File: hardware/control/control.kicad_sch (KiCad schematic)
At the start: 46 parts, among them IC1 TMUX4053DYYR, J0 43045-0412, J1 Conn_01x02_Pin, J11 Conn_01x04_Pin, J12 Camera Isolated triggers (ope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, J2 Conn_01x02_Pin, J3 Conn_01x02_Pin, J4 Conn_01x02_Pin, J5 Conn_01x05_Pin, J6 Conn_01x04_Pin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

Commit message: removing old thermocouple ic
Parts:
- removed C3: 0.1uF, Capacitor_THT:C_Disc_D5.0mm_W2.5mm_P2.50mm, symbol Device:C
- removed J7: Screw_Terminal_01x02, TerminalBlock_Phoenix:TerminalBlock_Phoenix_MKDS-1,5-2_1x02_P5.00mm_Horizontal, symbol Connector:Screw_Terminal_01x02
- removed U3: MAX6675ISA_, MAX6675ISA_:SOIC127P600X175-8N, symbol MAX6675ISA_:MAX6675ISA_
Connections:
- no-connect marks 18 -> 17
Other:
- note removed: "K-Thermocouple- to-Digital Converter"
- moved on the sheet: TP5

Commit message: external spi temp chip
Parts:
- added J7: Conn_01x08_Pin, Connector_Molex:Molex_PicoBlade_53047-0810_1x08_P1.25mm_Vertical, symbol Connector:Conn_01x08_Pin
- added R11: 10k, Resistor_THT:R_Axial_DIN0207_L6.3mm_D2.5mm_P10.16mm_Horizontal, symbol Device:R
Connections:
- net +5V: now also J7.4 (Pin_4)
- net GND: now also J7.2 (Pin_2), J7.5 (Pin_5), J7.7 (Pin_7)
- net at A1.13 (D10): now also J7.6 (Pin_6)
- net at A1.14 (MOSI): now also J7.8 (Pin_8), R11.2
- net at A1.15 (MISO): now also R11.1
- net at A1.16 (SCK): now also J7.1 (Pin_1)
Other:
- moved on the sheet: J6, TP6

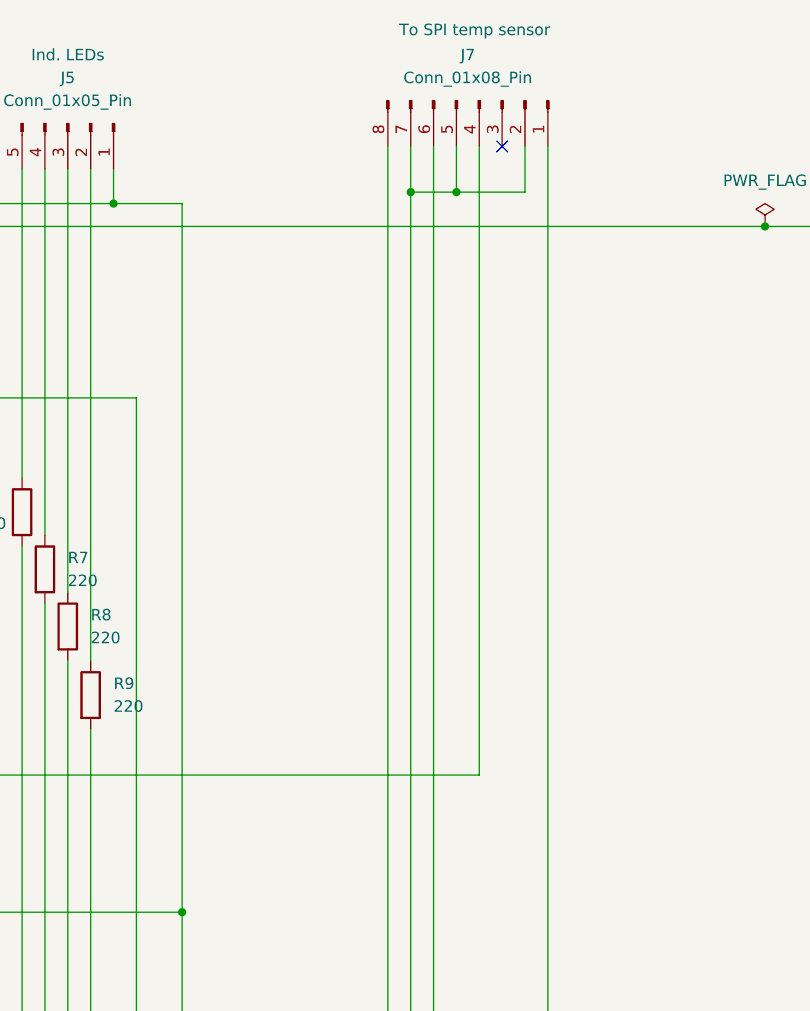
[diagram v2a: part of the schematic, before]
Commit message: added alert pullup
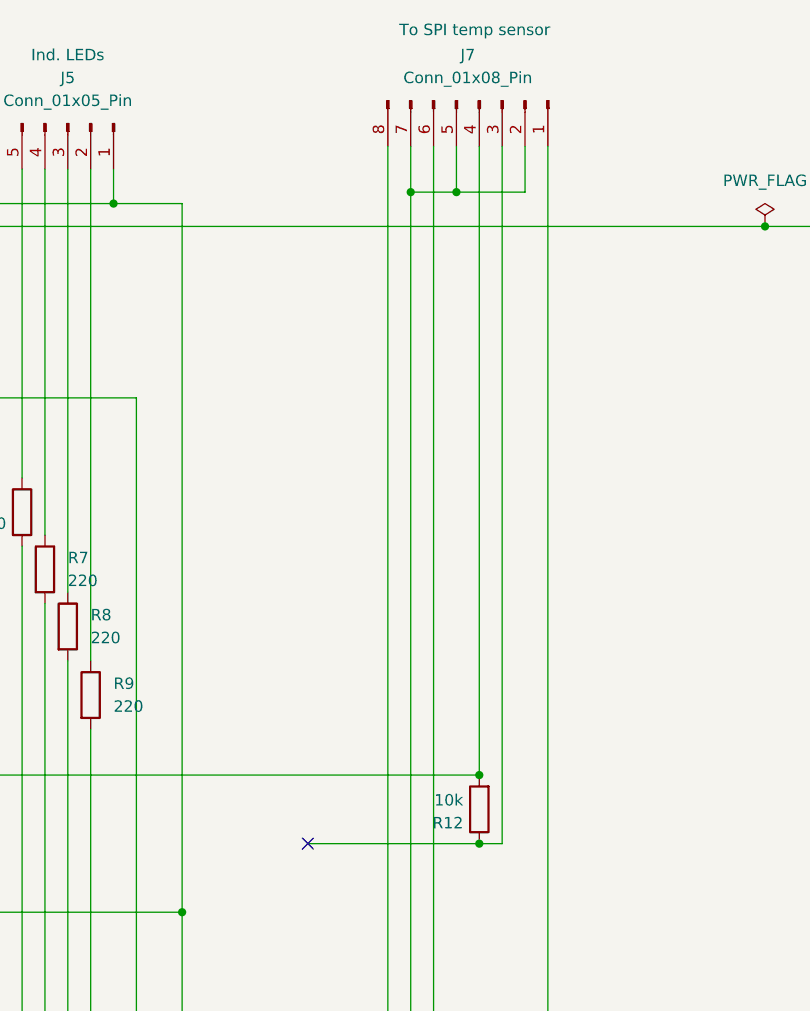
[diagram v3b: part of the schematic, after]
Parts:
- added R12: 10k, Resistor_THT:R_Axial_DIN0207_L6.3mm_D2.5mm_P10.16mm_Horizontal, symbol Device:R
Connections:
- net +5V: now also R12.2
- net at J7.3 (Pin_3): now also R12.1
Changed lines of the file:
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@@
 	)
 	(junction
+		(at 346.71 106.68)
+		(diameter 0)
+		(color 0 0 0 0)
+	)
+	(junction
 		(at 232.41 158.75)
 		(diameter 0)
@@
 	)
 	(junction
+		(at 346.71 99.06)
+		(diameter 0)
+		(color 0 0 0 0)
+	)
+	(junction
 		(at 203.2 118.11)
 		(diameter 0)
@@
 	)
 	(no_connect
-		(at 349.25 29.21)
-	)
-	(no_connect
 		(at 267.97 153.67)
 	)
@@
 	)
 	(no_connect
+		(at 327.66 106.68)
+	)
+	(no_connect
 		(at 261.62 31.75)
 	)
@@
 	(wire
 		(pts
+			(xy 327.66 106.68) (xy 346.71 106.68)
+		)
+		(stroke
+			(width 0)
+			(type default)
+		)
+	)
+	(wire
+		(pts
 			(xy 69.85 96.52) (xy 69.85 97.79)
 		)
@@
 	(wire
 		(pts
+			(xy 349.25 29.21) (xy 349.25 106.68)
+		)
+		(stroke
+			(width 0)
+			(type default)
+		)
+	)
+	(wire
+		(pts
 			(xy 378.46 38.1) (xy 386.08 38.1)
 		)
@@
 	(wire
 		(pts
+			(xy 349.25 106.68) (xy 346.71 106.68)
+		)
+		(stroke
+			(width 0)
+			(type default)
+		)
+	)
+	(wire
+		(pts
 			(xy 232.41 158.75) (xy 252.73 158.75)
 		)
@@
 					(unit 1)
 				)
+			)
+		)
+	)
+	(symbol
+		(lib_id "Device:R")
+		(at 346.71 102.87 180)
+		(unit 1)
+		(body_style 1)
+		(exclude_from_sim no)
+		(in_bom yes)
+		(on_board yes)
+		(in_pos_files yes)
+		(dnp no)
+		(property "Reference" "R12"
+			(at 344.932 104.394 0)
+			(show_name no)
+			(do_not_autoplace no)
+			(effects
+				(font
+					(size 1.27 1.27)
+				)
+				(justify left)
+			)
+		)
+		(property "Value" "10k"
+			(at 344.932 101.854 0)
+			(show_name no)
+			(do_not_autoplace no)
+			(effects
+				(font
+					(size 1.27 1.27)
+				)
+				(justify left)
+			)
+		)
+		(property "Footprint" "Resistor_THT:R_Axial_DIN0207_L6.3mm_D2.5mm_P10.16mm_Horizontal"
+			(at 348.488 102.87 90)
+			(hide yes)
+			(show_name no)
+			(do_not_autoplace no)
+			(effects
+				(font
+					(size 1.27 1.27)
+				)
+			)
+		)
+		(property "Datasheet" ""
+			(at 346.71 102.87 0)
+			(hide yes)
+			(show_name no)
+			(do_not_autoplace no)
+			(effects
+				(font
+					(size 1.27 1.27)
+				)
+			)
+		)
+		(property "Description" ""
+			(at 346.71 102.87 0)
+			(show_name no)
+			(do_not_autoplace no)
+			(effects
+				(font
+					(size 1.27 1.27)
+				)
+			)
+		)
+		(pin "2"
+		)
+		(pin "1"
+		)
+		(instances
+			(project "control"
+				(path "/22c636c5-bb06-4895-803e-d0c20393f5d8"
+					(reference "R12")
+					(unit 1)
+				)

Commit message: rework pcb layout
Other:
- moved on the sheet: F1, J0, TP2

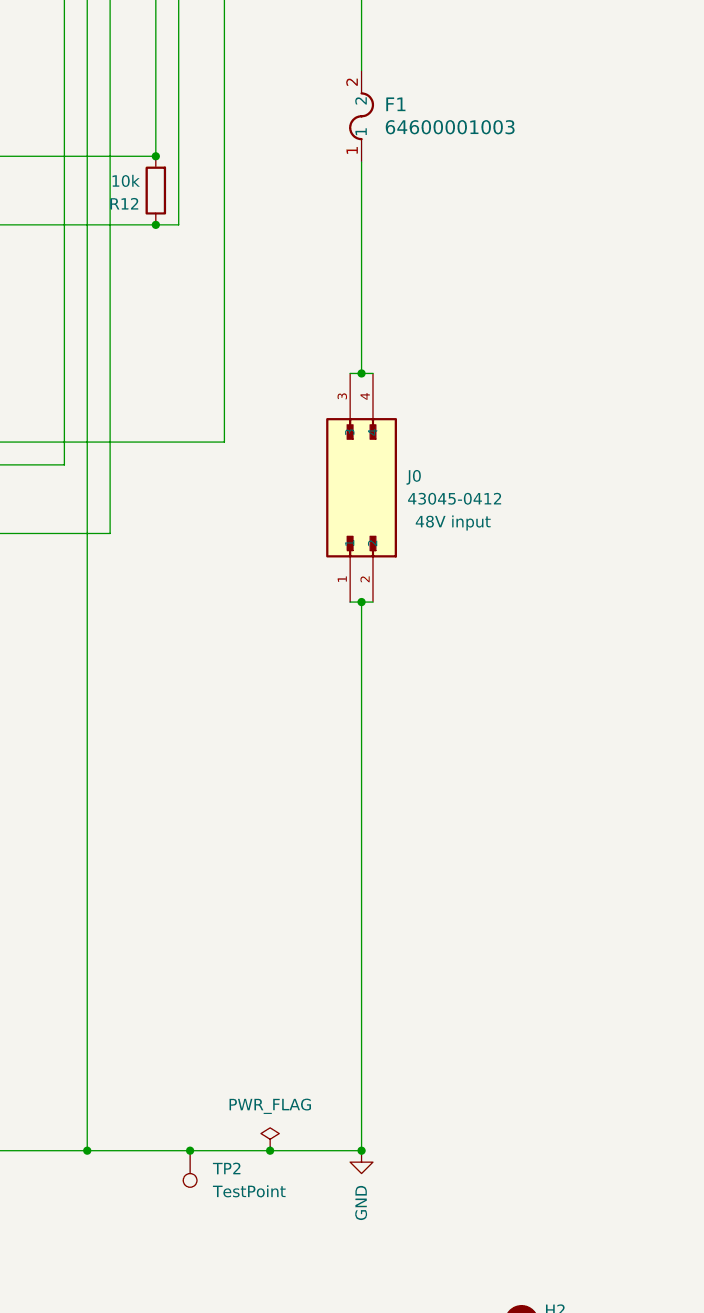
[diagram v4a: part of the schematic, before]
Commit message: changed molex connector
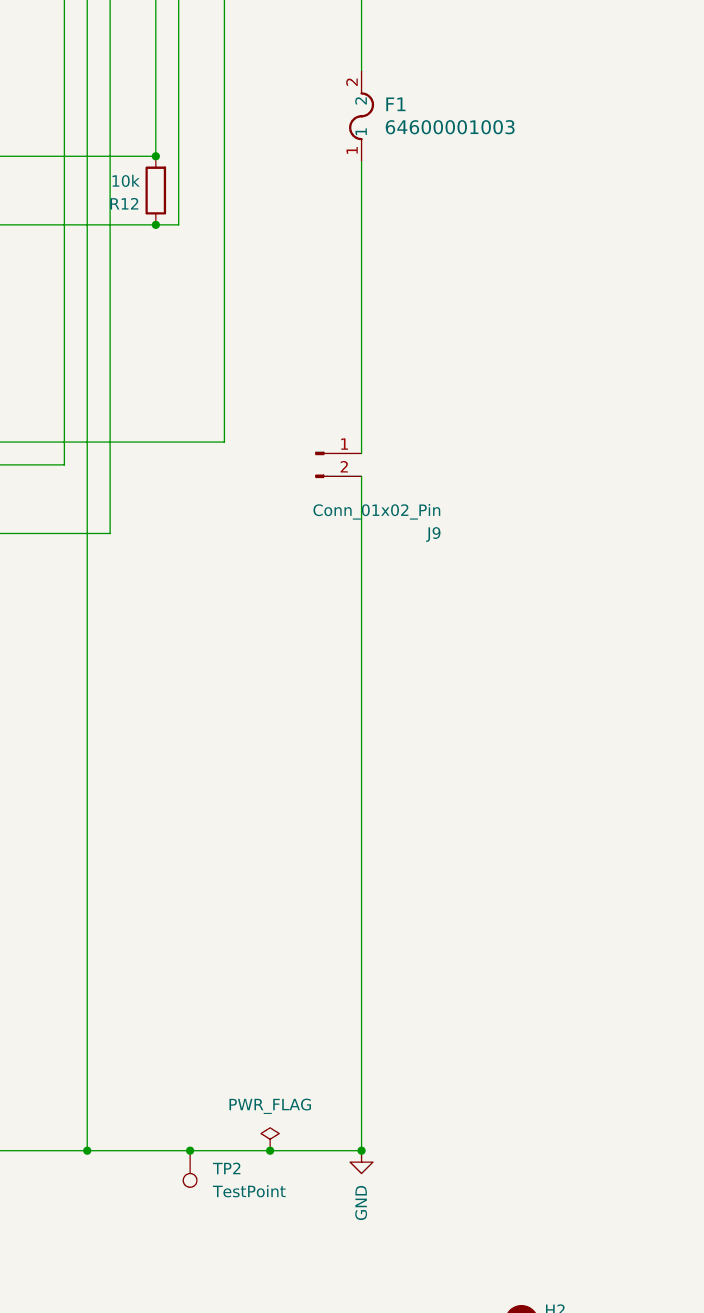
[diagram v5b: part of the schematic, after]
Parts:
- removed J0: 43045-0412, 43045-0412:MOLEX_43045-0412, symbol 43045-0412:43045-0412
- added J9: Conn_01x02_Pin, Connector_Molex:Molex_Micro-Fit_3.0_43650-0215_1x02_P3.00mm_Vertical, symbol Connector:Conn_01x02_Pin
- J1, J2, J3, J4: footprint molex_0436500215:Molex_Micro-Fit_3.0_43650-0215_1x02_P3.00mm_Vertical -> Connector_Molex:Molex_Micro-Fit_3.0_43650-0215_1x02_P3.00mm_Vertical
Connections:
- net GND: now also J9.2 (Pin_2)
- net at F1.1: now also J9.1 (Pin_1)
